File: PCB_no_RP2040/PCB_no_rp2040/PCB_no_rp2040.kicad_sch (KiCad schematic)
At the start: 102 parts, among them J1 02x30_Shift_Register_Connector, J2 02x30_ADC_Connector, U1 74HC595, U2 74HC595, U3 74HC595, U4 74HC595, U5 74HC595, U6 74HC595, U7 74HC595, U8 MAX11643EEG, U9 MAX11643EEG

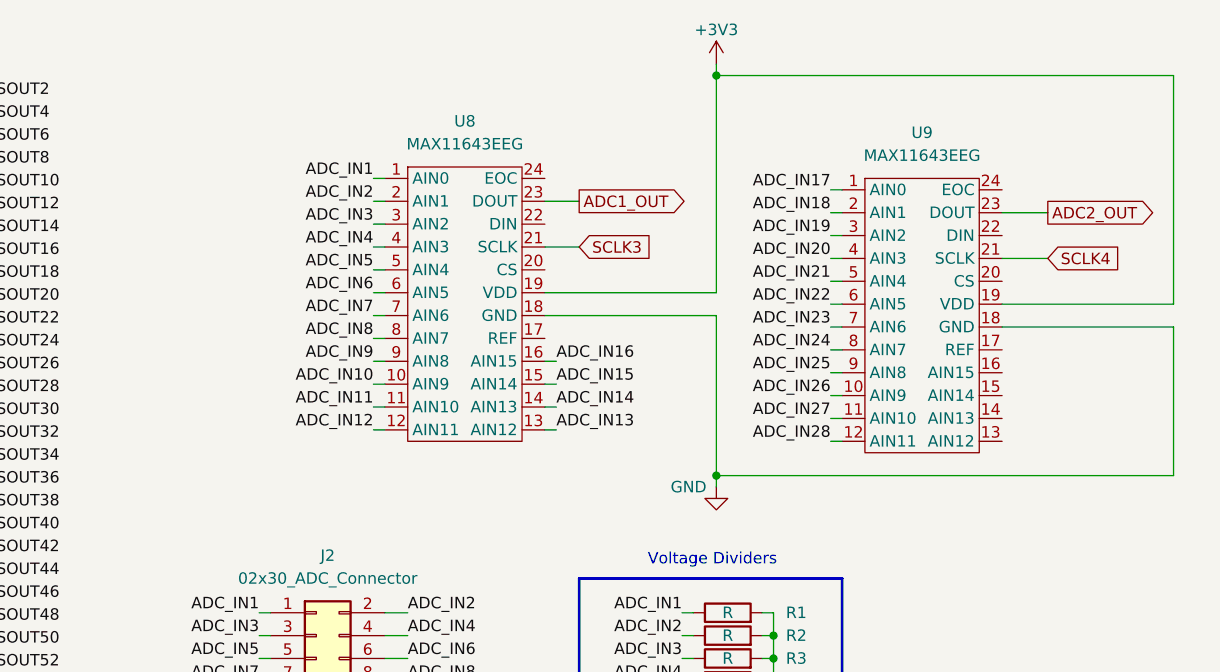
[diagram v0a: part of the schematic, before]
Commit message: added decouple caps for the ADCs
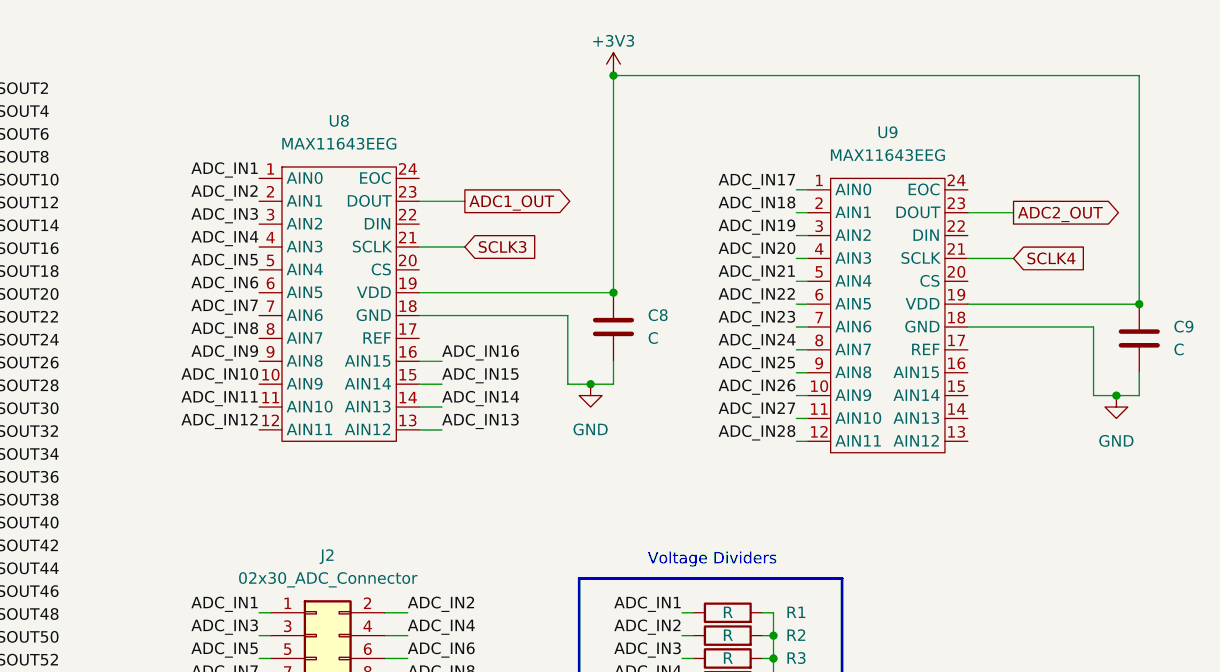
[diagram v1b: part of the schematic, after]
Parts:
- added C8, C9: C, symbol Device:C
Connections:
- net +3V3: now also C8.1, C9.1
- net GND: now also C8.2, C9.2
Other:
- moved on the sheet: U8, U9

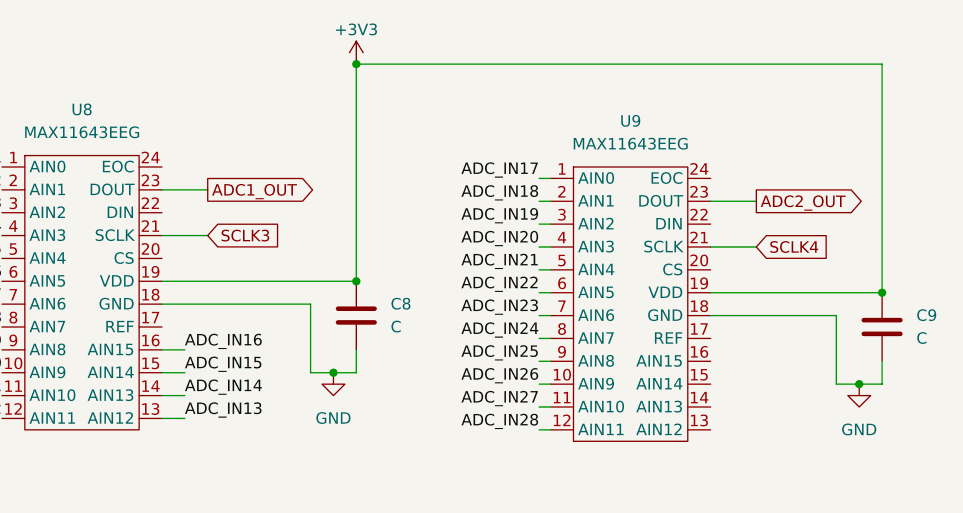
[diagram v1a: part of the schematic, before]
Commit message: Changed adc connections to honor SPI
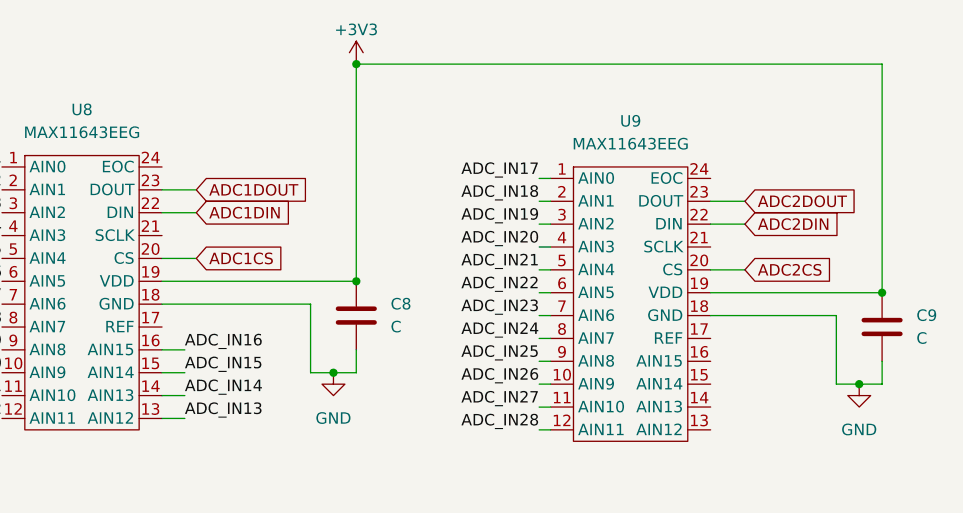
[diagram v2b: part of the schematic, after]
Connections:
- net ADC2CS: now reaches U9.20 (CS)
- net ADC2DIN: now reaches U9.22 (DIN)
- net ADC1CS: now reaches U8.20 (CS)
- net ADC1DIN: now reaches U8.22 (DIN)
- net ADC1_OUT renamed ADC1DOUT
- net ADC2_OUT renamed ADC2DOUT
- net SCLK3: no longer names the net of U8.21 (SCLK)
- net SCLK4: no longer names the net of U9.21 (SCLK)
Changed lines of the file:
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@@
+    (stroke (width 0) (type default))
+  )
+  (wire (pts (xy 261.62 34.29) (xy 257.81 34.29))
     (stroke (width 0) (type default))
   )
@@
     (stroke (width 0) (type default))
   )
+  (wire (pts (xy 200.66 33.02) (xy 196.85 33.02))
+    (stroke (width 0) (type default))
+  )
   (wire (pts (xy 71.12 30.48) (xy 72.39 30.48))
     (stroke (width 0) (type default))
@@
     (stroke (width 0) (type default))
   )
-  (wire (pts (xy 257.81 34.29) (xy 262.89 34.29))
-    (stroke (width 0) (type default))
-  )
   (wire (pts (xy 234.95 101.6) (xy 236.22 101.6))
     (stroke (width 0) (type default))
@@
     (stroke (width 0) (type default))
   )
+  (wire (pts (xy 200.66 35.56) (xy 196.85 35.56))
+    (stroke (width 0) (type default))
+  )
   (wire (pts (xy 226.06 88.9) (xy 227.33 88.9))
     (stroke (width 0) (type default))
@@
     (stroke (width 0) (type default))
   )
-  (wire (pts (xy 201.93 38.1) (xy 196.85 38.1))
-    (stroke (width 0) (type default))
-  )
   (wire (pts (xy 226.06 129.54) (xy 227.33 129.54))
     (stroke (width 0) (type default))
@@
     (stroke (width 0) (type default))
   )
+  (wire (pts (xy 261.62 41.91) (xy 257.81 41.91))
+    (stroke (width 0) (type default))
+  )
   (wire (pts (xy 92.71 38.1) (xy 105.41 38.1))
     (stroke (width 0) (type default))
@@
     (stroke (width 0) (type default))
   )
+  (wire (pts (xy 261.62 36.83) (xy 257.81 36.83))
+    (stroke (width 0) (type default))
+  )
   (wire (pts (xy 116.84 82.55) (xy 118.11 82.55))
     (stroke (width 0) (type default))
@@
     (stroke (width 0) (type default))
   )
+  (wire (pts (xy 200.66 40.64) (xy 196.85 40.64))
+    (stroke (width 0) (type default))
+  )
   (wire (pts (xy 92.71 78.74) (xy 105.41 78.74))
     (stroke (width 0) (type default))
@@
     (stroke (width 0) (type default))
   )
-  (wire (pts (xy 257.81 39.37) (xy 262.89 39.37))
-    (stroke (width 0) (type default))
-  )
   (wire (pts (xy 125.73 39.37) (xy 127 39.37))
     (stroke (width 0) (type default))
@@
   )
   (wire (pts (xy 140.97 41.91) (xy 139.7 41.91))
-    (stroke (width 0) (type default))
-  )
-  (wire (pts (xy 201.93 33.02) (xy 196.85 33.02))
     (stroke (width 0) (type default))
   )
@@
     )
   )
-  (global_label "ADC2_OUT" (shape output) (at 262.89 34.29 0) (fields_autoplaced)
-    (effects (font (size 1.27 1.27)) (justify left))
-    (property "Intersheetrefs" "${INTERSHEET_REFS}" (at 275.3095 34.29 0)
+  (global_label "ADC2DIN" (shape input) (at 261.62 36.83 0) (fields_autoplaced)
+    (effects (font (size 1.27 1.27)) (justify left))
+    (property "Intersheetrefs" "${INTERSHEET_REFS}" (at 272.6486 36.83 0)
+      (effects (font (size 1.27 1.27)) (justify left) hide)
+    )
+  )
+  (global_label "ADC2DOUT" (shape input) (at 261.62 34.29 0) (fields_autoplaced)
+    (effects (font (size 1.27 1.27)) (justify left))
+    (property "Intersheetrefs" "${INTERSHEET_REFS}" (at 274.3419 34.29 0)
       (effects (font (size 1.27 1.27)) (justify left) hide)
     )
@@
     )
   )
-  (global_label "ADC1_OUT" (shape output) (at 201.93 33.02 0) (fields_autoplaced)
-    (effects (font (size 1.27 1.27)) (justify left))
-    (property "Intersheetrefs" "${INTERSHEET_REFS}" (at 214.3495 33.02 0)
+  (global_label "ADC1DOUT" (shape input) (at 200.66 33.02 0) (fields_autoplaced)
+    (effects (font (size 1.27 1.27)) (justify left))
+    (property "Intersheetrefs" "${INTERSHEET_REFS}" (at 213.3819 33.02 0)
+      (effects (font (size 1.27 1.27)) (justify left) hide)
+    )
+  )
+  (global_label "ADC1DIN" (shape input) (at 200.66 35.56 0) (fields_autoplaced)
+    (effects (font (size 1.27 1.27)) (justify left))
+    (property "Intersheetrefs" "${INTERSHEET_REFS}" (at 211.6886 35.56 0)
       (effects (font (size 1.27 1.27)) (justify left) hide)
     )
@@
     )
   )
+  (global_label "ADC2CS" (shape input) (at 261.62 41.91 0) (fields_autoplaced)
+    (effects (font (size 1.27 1.27)) (justify left))
+    (property "Intersheetrefs" "${INTERSHEET_REFS}" (at 271.9228 41.91 0)
+      (effects (font (size 1.27 1.27)) (justify left) hide)
+    )
+  )
   (global_label "OE1" (shape input) (at 50.8 128.27 0) (fields_autoplaced)
     (effects (font (size 1.27 1.27)) (justify left))
@@
     )
   )
-  (global_label "SCLK3" (shape input) (at 201.93 38.1 0) (fields_autoplaced)
-    (effects (font (size 1.27 1.27)) (justify left))
-    (property "Intersheetrefs" "${INTERSHEET_REFS}" (at 210.9023 38.1 0)
-      (effects (font (size 1.27 1.27)) (justify left) hide)
-    )
-  )
   (global_label "OE1" (shape input) (at 50.8 87.63 0) (fields_autoplaced)
     (effects (font (size 1.27 1.27)) (justify left))
@@
     )
   )
+  (global_label "ADC1CS" (shape input) (at 200.66 40.64 0) (fields_autoplaced)
+    (effects (font (size 1.27 1.27)) (justify left))
+    (property "Intersheetrefs" "${INTERSHEET_REFS}" (at 210.9628 40.64 0)
+      (effects (font (size 1.27 1.27)) (justify left) hide)
+    )
+  )
   (global_label "RCLK1" (shape input) (at 48.26 124.46 0) (fields_autoplaced)
     (effects (font (size 1.27 1.27)) (justify left))
@@
       (effects (font (size 1.27 1.27)) (justify left) hide)
     )
-  )
-  (global_label "SCLK4" (shape input) (at 262.89 39.37 0) (fields_autoplaced)
-    (effects (font (size 1.27 1.27)) (justify left))
-    (property "Intersheetrefs" "${INTERSHEET_REFS}" (at 271.8623 39.37 0)
-      (effects (font (size 1.27 1.27)) (justify left) hide)
-    )
